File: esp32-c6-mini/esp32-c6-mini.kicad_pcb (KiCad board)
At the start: 2 copper layers, 1 part, among them U1 ESP32-C6-MINI-1-N4

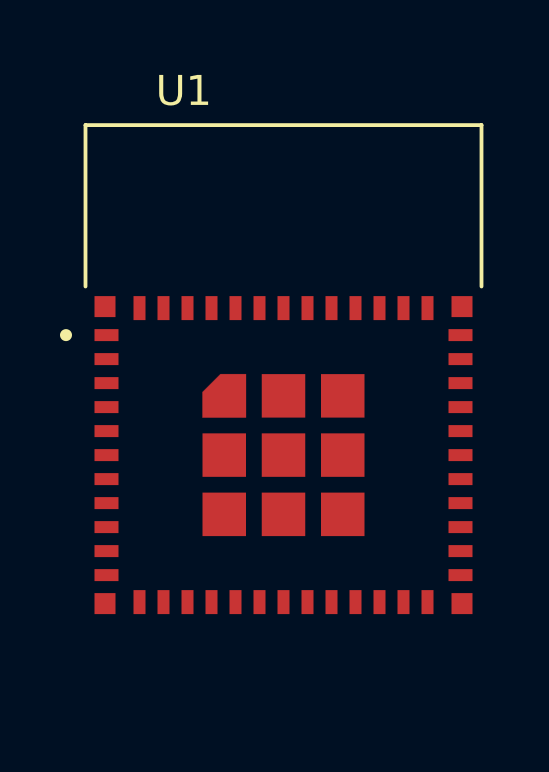
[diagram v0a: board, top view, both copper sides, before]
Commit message: fix: use official espressif lib for esp32-c6 projects
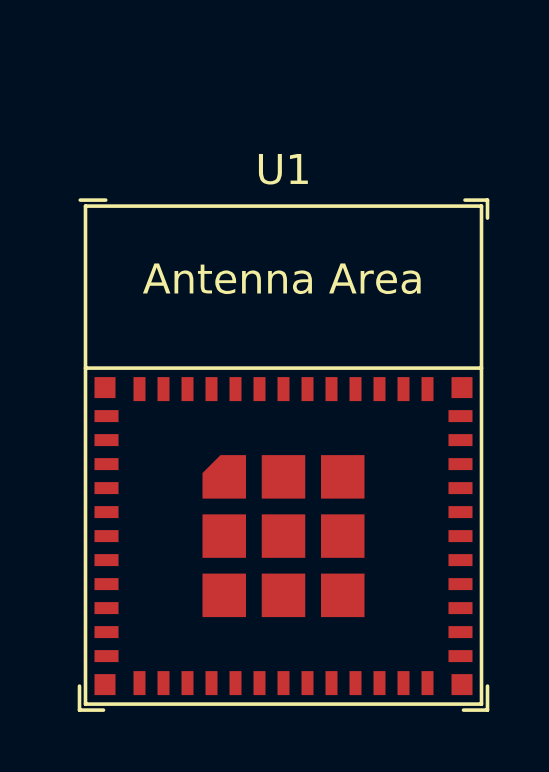
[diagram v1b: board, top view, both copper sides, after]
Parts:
- U1: value ESP32-C6-MINI-1-N4 -> ESP32-C6-MINI-1/U; footprint ESP32:XCVR_ESP32-C6-MINI-1-N4 -> PCM_Espressif:ESP32-C6-MINI-1
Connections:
- U1 pad 1: GND1 -> Net-(U1-GND-Pad1)
- U1 pad 11: GND1 -> Net-(U1-GND-Pad1)
- U1 pad 14: GND1 -> Net-(U1-GND-Pad1)
- U1 pad 2: GND1 -> Net-(U1-GND-Pad1)
- U1 pad 36: GND1 -> Net-(U1-GND-Pad1)
- U1 pad 37: GND1 -> Net-(U1-GND-Pad1)
- U1 pad 38: GND1 -> Net-(U1-GND-Pad1)
- U1 pad 39: GND1 -> Net-(U1-GND-Pad1)
- U1 pad 40: GND1 -> Net-(U1-GND-Pad1)
- U1 pad 41: GND1 -> Net-(U1-GND-Pad1)
- U1 pad 42: GND1 -> Net-(U1-GND-Pad1)
- U1 pad 43: GND1 -> Net-(U1-GND-Pad1)
- U1 pad 44: GND1 -> Net-(U1-GND-Pad1)
- U1 pad 45: GND1 -> Net-(U1-GND-Pad1)
- U1 pad 46: GND1 -> Net-(U1-GND-Pad1)
- U1 pad 47: GND2 -> Net-(U1-GND-Pad1)
- U1 pad 48: GND2 -> Net-(U1-GND-Pad1)
- U1 pad 50: GND2 -> Net-(U1-GND-Pad1)
- U1 pad 51: GND2 -> Net-(U1-GND-Pad1)
- U1 pad 52: GND2 -> Net-(U1-GND-Pad1)
- U1 pad 53: GND2 -> Net-(U1-GND-Pad1)
